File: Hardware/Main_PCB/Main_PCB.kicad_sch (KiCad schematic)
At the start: 5 parts, among them J1 RC receiver, U1 ICM-42688-P

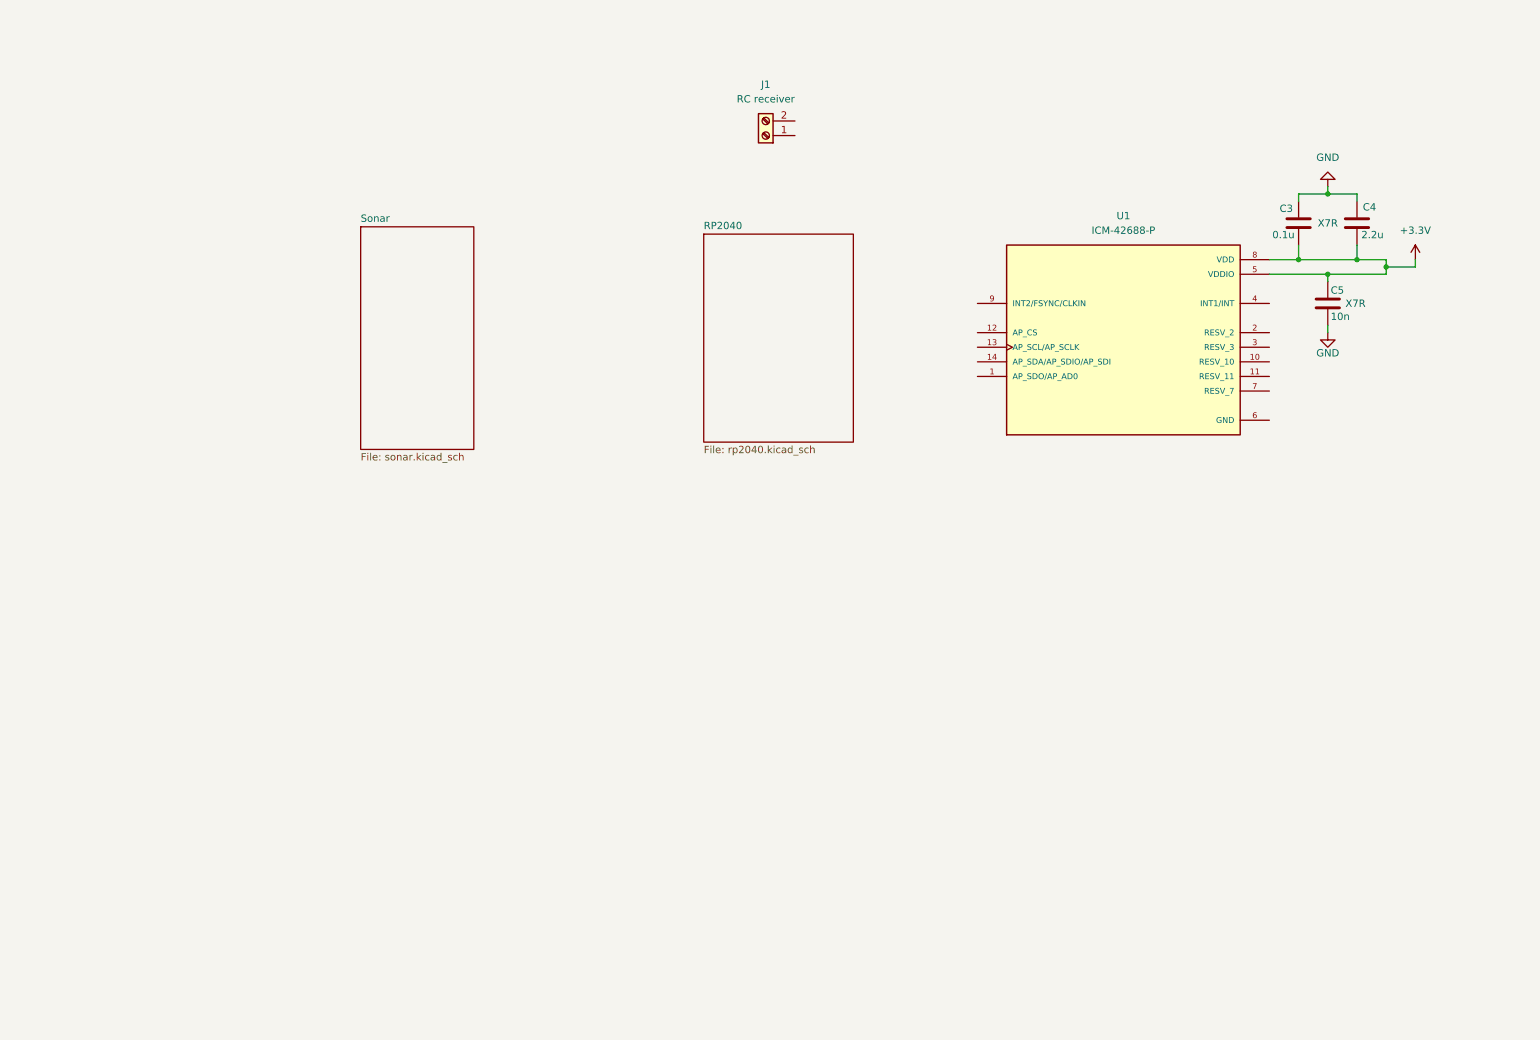
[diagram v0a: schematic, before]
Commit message: Added Buck and Boost converter as well as a basic RP2040 circuit
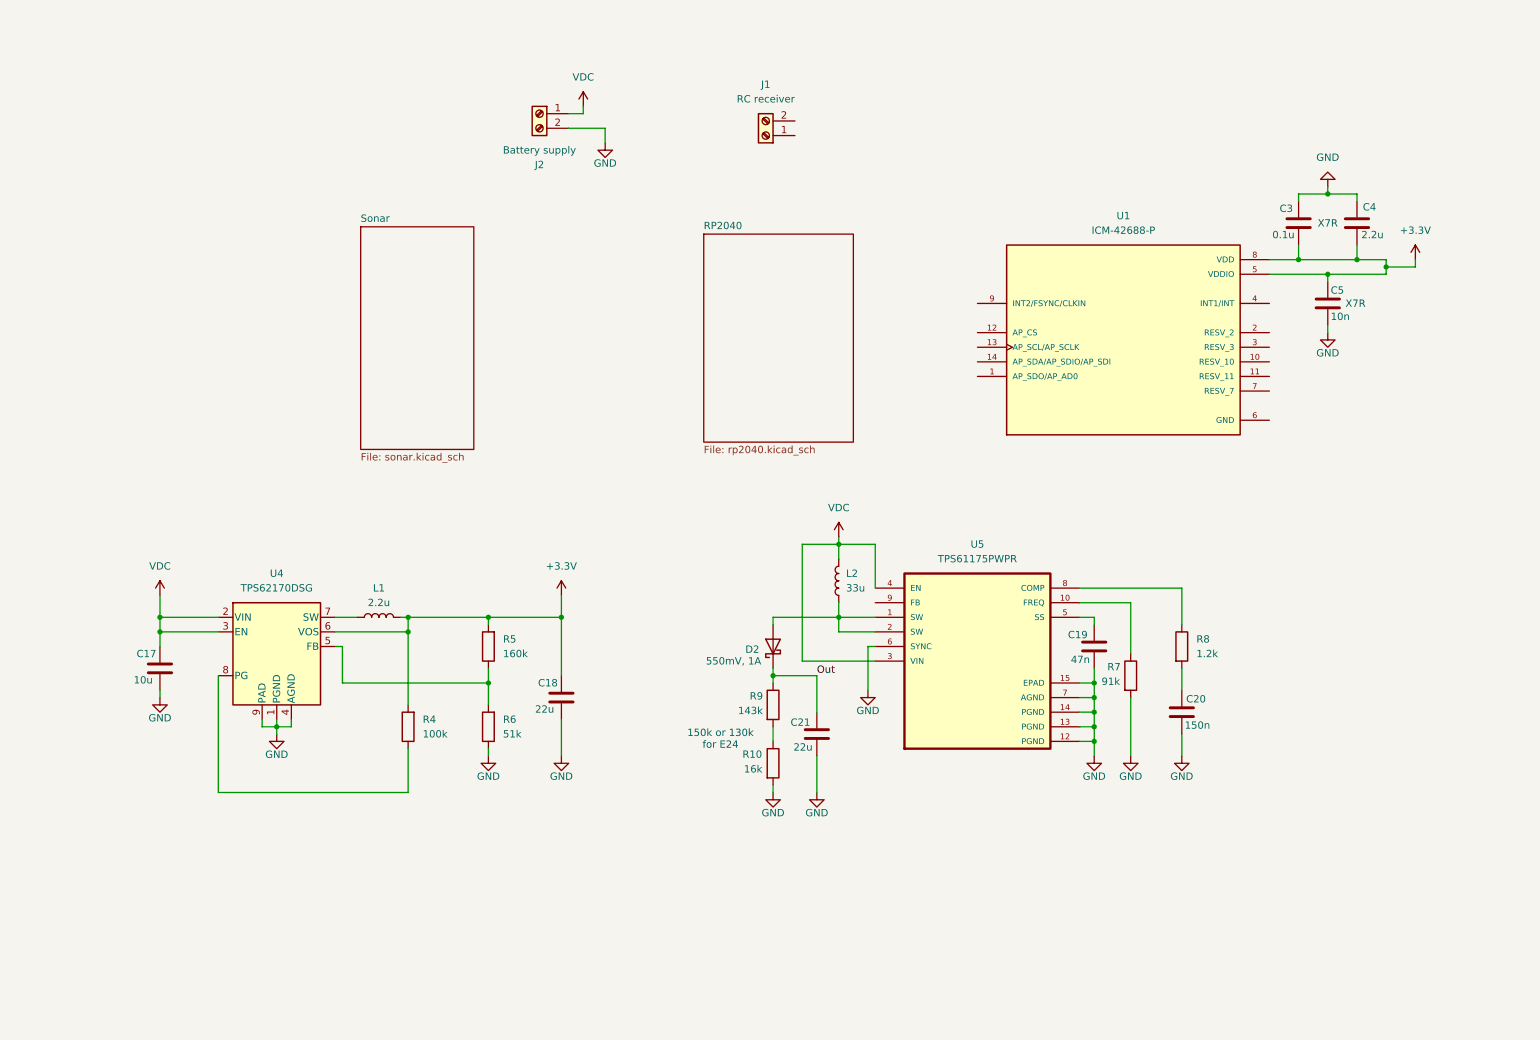
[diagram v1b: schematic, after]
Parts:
- added C17: 10u, symbol Device:C
- added C18, C21: 22u, symbol Device:C
- added C19: 47n, symbol Device:C
- added C20: 150n, symbol Device:C
- added D2: 550mV, 1A, symbol Device:D_Schottky
- added J2: Battery supply, symbol Connector:Screw_Terminal_01x02
- added L1: 2.2u, symbol Device:L
- added L2: 33u, symbol Device:L
- added R10: 16k, symbol Device:R
- added R4: 100k, symbol Device:R
- added R5: 160k, symbol Device:R
- added R6: 51k, symbol Device:R
- added R7: 91k, symbol Device:R
- added R8: 1.2k, symbol Device:R
- added R9: 143k, symbol Device:R
- added U4: TPS62170DSG, Package_SON:WSON-8-1EP_2x2mm_P0.5mm_EP0.9x1.6mm_ThermalVias, symbol Regulator_Switching:TPS62170DSG
- added U5: TPS61175PWPR, TPS61175PWPR:IC_TPS27S100BPWPR, symbol TPS61175PWPR:TPS61175PWPR
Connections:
- net +3.3V: now also C18.1, L1.2, R4.2, R5.2, U4.6 (VOS)
- net GND: now also C17.2, C18.2, C19.2, C20.2, C21.2, J2.2 (Pin_2), R10.2, R6.1, R7.2, U4.1 (PGND), U4.4 (AGND), U4.9 (PAD), U5.12 (PGND), U5.13 (PGND), U5.14 (PGND), U5.15 (EPAD), U5.6 (SYNC), U5.7 (AGND)
- new net: R7.1, U5.10 (FREQ)
- new net: R4.1, U4.8 (PG)
- new net: R10.1, R9.2
- new net: R5.1, R6.2, U4.5 (FB)
- new net: L1.1, U4.7 (SW)
- new net: C19.1, U5.5 (SS)
- new net: D2.2 (A), L2.1, U5.1 (SW), U5.2 (SW)
- new net: R8.1, U5.8 (COMP)
- new net: C20.1, R8.2
- new net Out: C21.1, D2.1 (K), R9.1
- new net VDC: C17.1, J2.1 (Pin_1), L2.2, U4.2 (VIN), U4.3 (EN), U5.3 (VIN), U5.4 (EN)
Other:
- note added: "150k or 130k for E24"

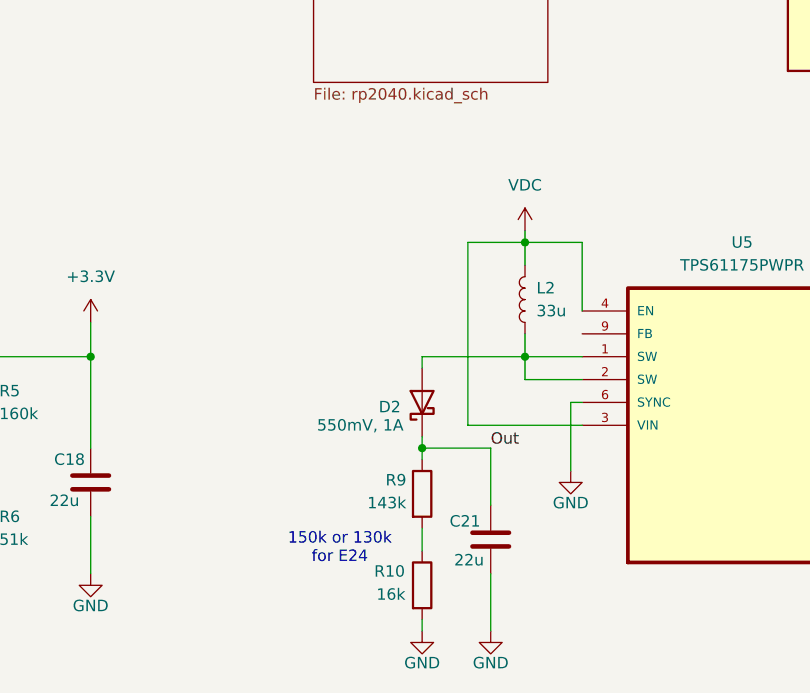
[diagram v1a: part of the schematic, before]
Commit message: Fixed stupid things on the boost converter
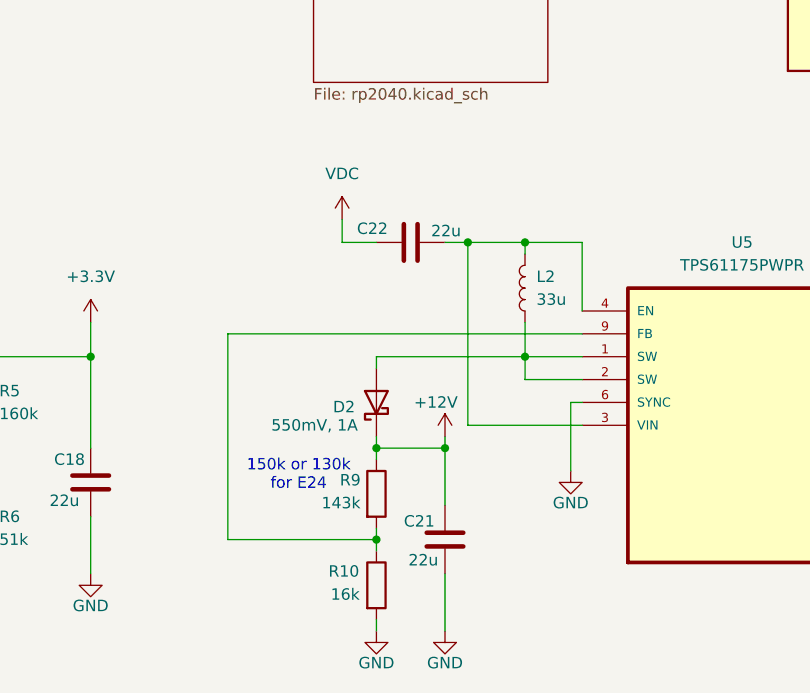
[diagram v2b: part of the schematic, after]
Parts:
- added C22: 22u, symbol Device:C
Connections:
- net VDC: now also C22.1; no longer L2.2, U5.3 (VIN), U5.4 (EN)
- net at R10.1, R9.2: now also U5.9 (FB)
- net Out renamed +12V
- new net: C22.2, L2.2, U5.3 (VIN), U5.4 (EN)
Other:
- moved on the sheet: C21, D2, L2, R10, R9

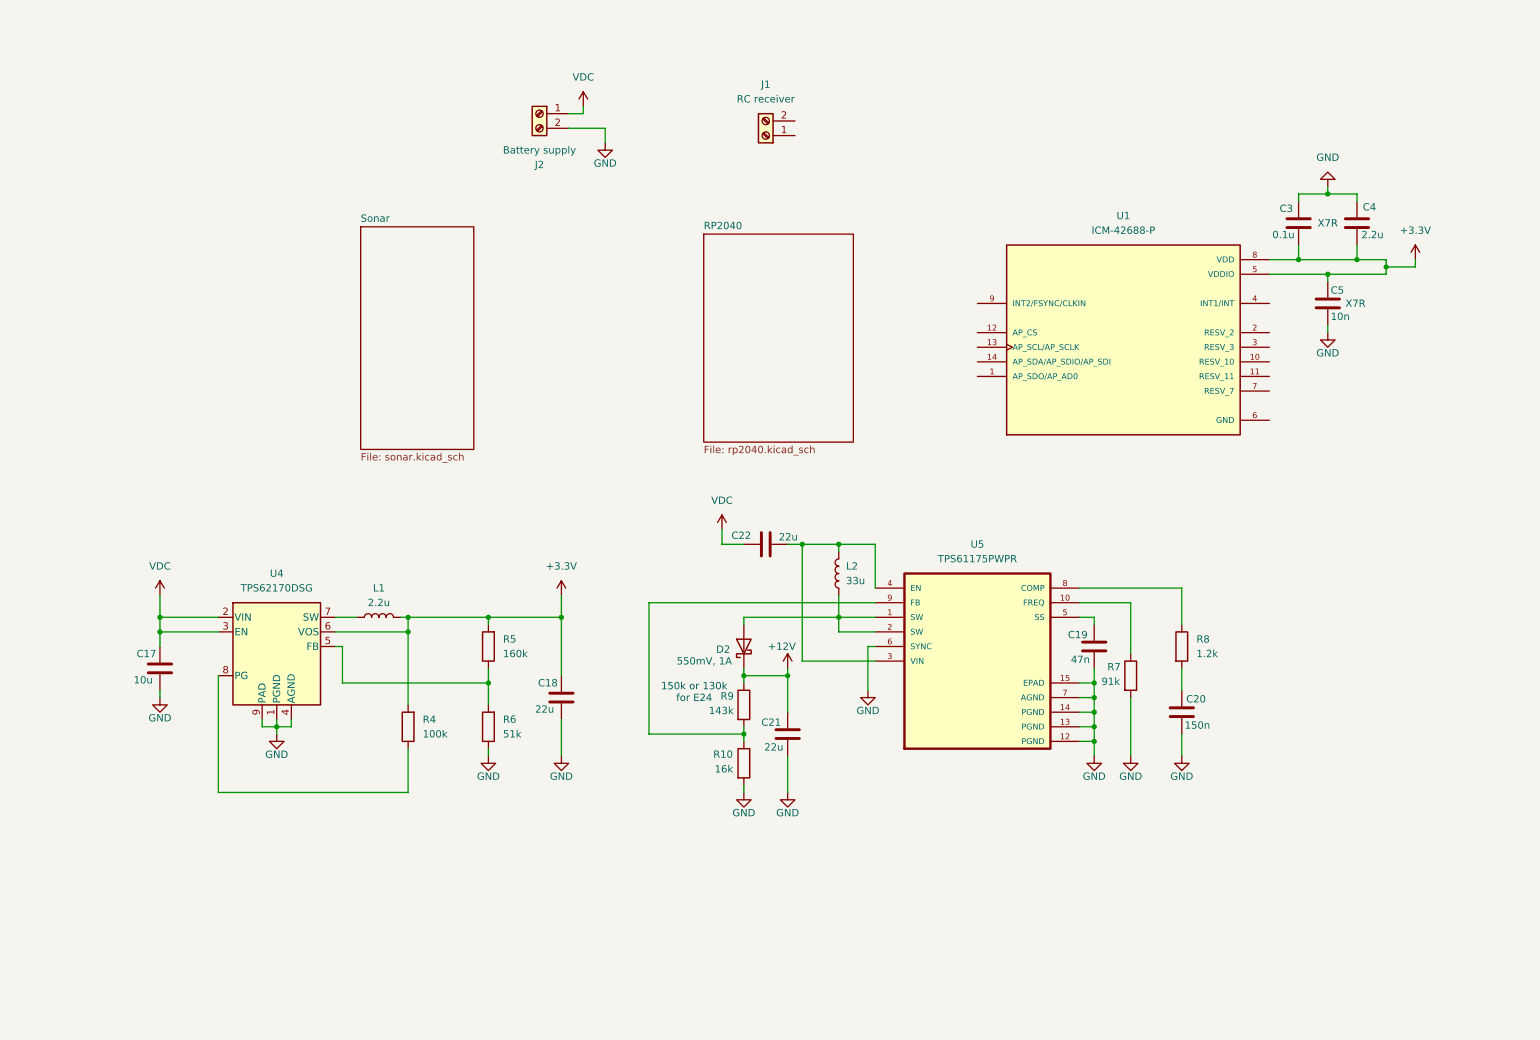
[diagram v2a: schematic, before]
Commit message: Trustworthy version of the MAIN PCB schematic
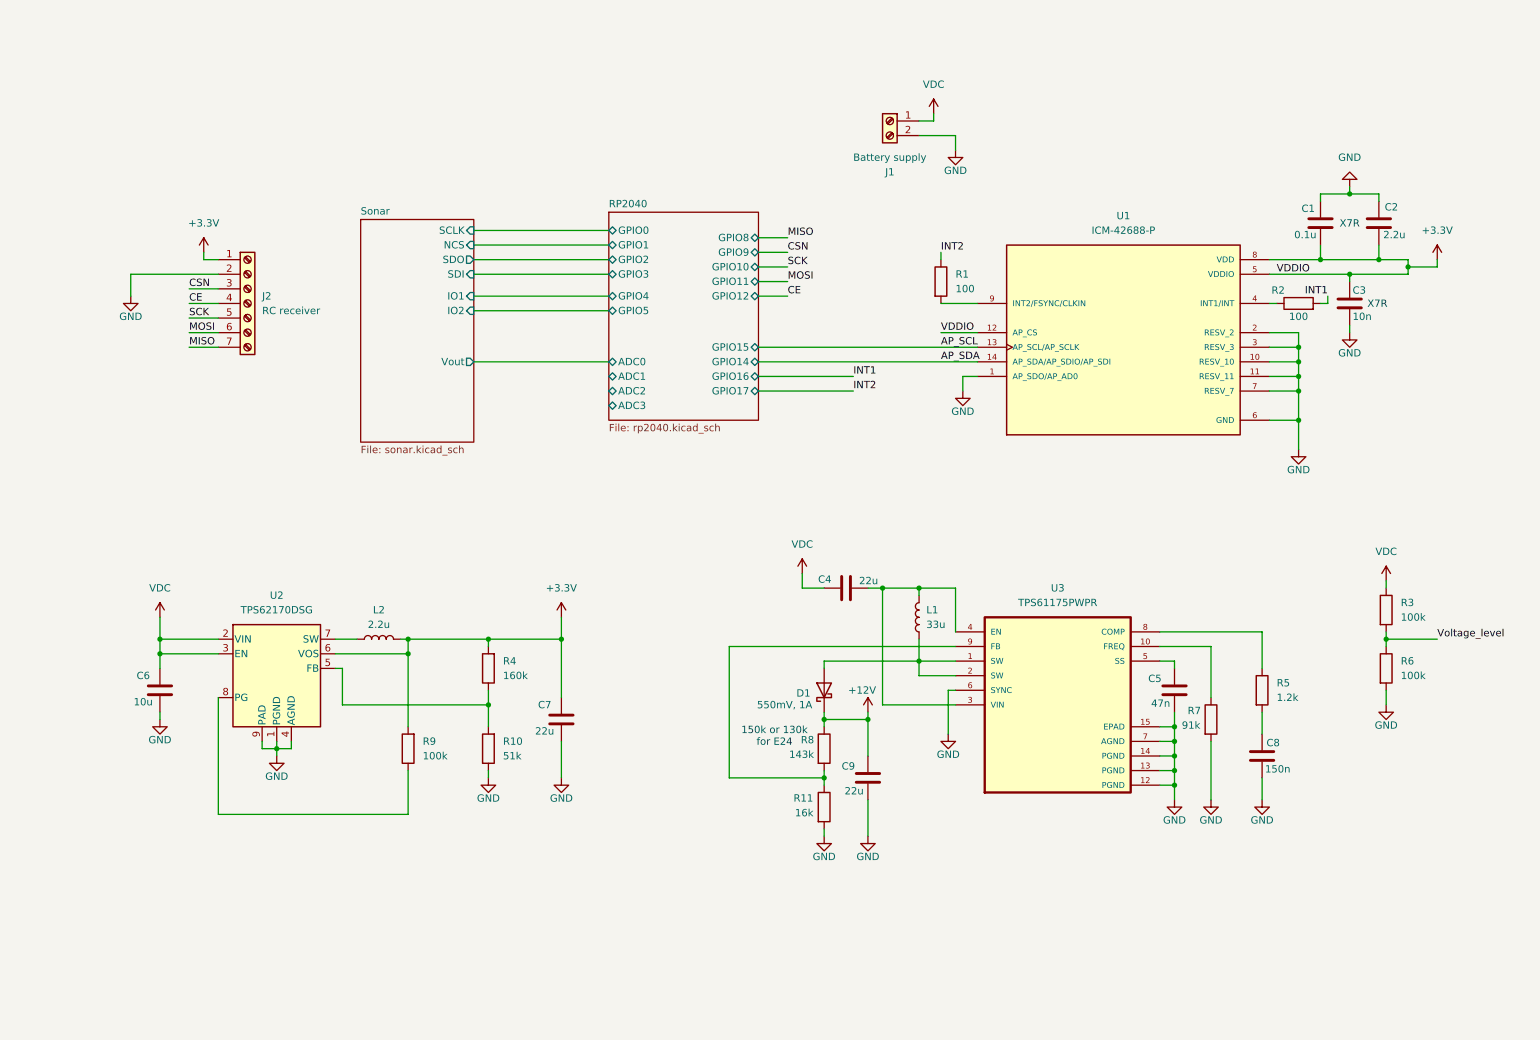
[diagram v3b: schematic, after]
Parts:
- removed J1: RC receiver, symbol Connector:Screw_Terminal_01x02
- added J2: RC receiver, symbol Connector:Screw_Terminal_01x07
- added R1, R2: 100, symbol Device:R
- added R3, R6: 100k, symbol Device:R
- renumbered C3 to C1, C4 to C2, C5 to C3, C22 to C4, C19 to C5, C17 to C6, C18 to C7, C20 to C8, C21 to C9, D2 to D1, J2 to J1, L2 to L1, L1 to L2, R6 to R10, R10 to R11, R5 to R4, R8 to R5, R9 to R8, R4 to R9, U4 to U2, U5 to U3
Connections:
- net +3.3V: now also U1.12 (AP_CS), J2.1 (Pin_1)
- net GND: now also U1.1 (AP_SDO/AP_AD0), U1.10 (RESV_10), U1.11 (RESV_11), U1.2 (RESV_2), U1.3 (RESV_3), U1.6 (GND), U1.7 (RESV_7), J2.2 (Pin_2), R6.2
- net VDC: now also R3.1
- net AP_SCL: now reaches U1.13 (AP_SCL/AP_SCLK)
- net AP_SDA: now reaches U1.14 (AP_SDA/AP_SDIO/AP_SDI)
- net at U1.4 (INT1/INT): now also R2.1
- net at U1.9 (INT2/FSYNC/CLKIN): now also R1.2
- new net CE: J2.4 (Pin_4)
- new net CSN: J2.3 (Pin_3)
- new net INT1: R2.2
- new net INT2: R1.1
- new net MISO: J2.7 (Pin_7)
- new net MOSI: J2.6 (Pin_6)
- new net SCK: J2.5 (Pin_5)
- new net Voltage_level: R3.2, R6.1
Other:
- sheet RP2040 ports: added ADC0, ADC1, ADC2, ADC3, GPIO0, GPIO1, GPIO10, GPIO11, GPIO12, GPIO14, GPIO15, GPIO16, GPIO17, GPIO2, GPIO3, GPIO4, GPIO5, GPIO8, GPIO9; removed none
- sheet Sonar ports: added IO1, IO2, NCS, SCLK, SDI, SDO, Vout; removed none
- moved on the sheet: C1, C2, C3, C4, C5, C6, C7, C8, C9, D1, J1, L1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
